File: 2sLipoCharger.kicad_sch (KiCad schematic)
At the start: 21 parts, among them IC1 CN3702, J2 Conn_01x03_Pin, Q2 PMOS, SW1 SW_SPDT

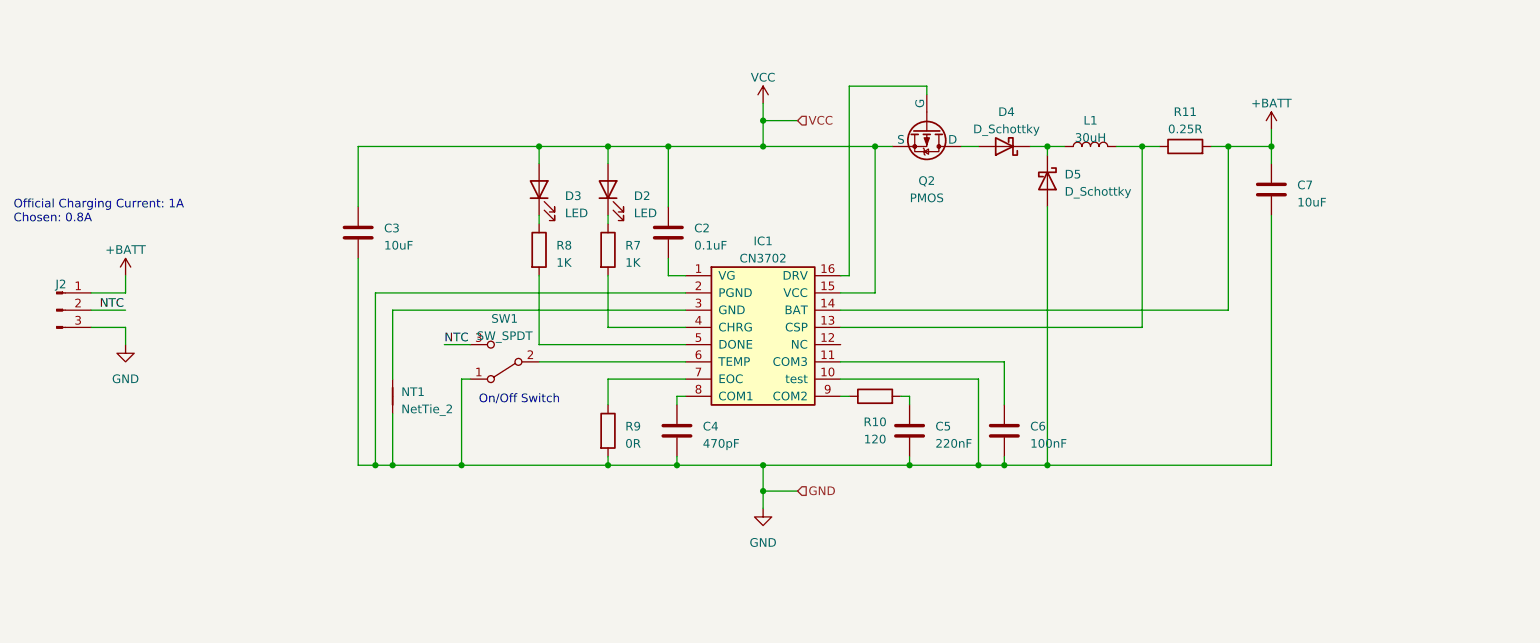
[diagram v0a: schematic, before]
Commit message: Finished Schematic
- Cleaned up page 1
- Only 3 chargers / board now
- LED no longer activated by PG, connected to VCC after the P-MOSFET instead
- Added DC barrel jack for daisy chaining (using M-M 30cm cable)

- Added jumper to enable fast charge
- Selected inductor, diode, P-MOSFET, current sense resistor
- Changed slide switch to 90 degree
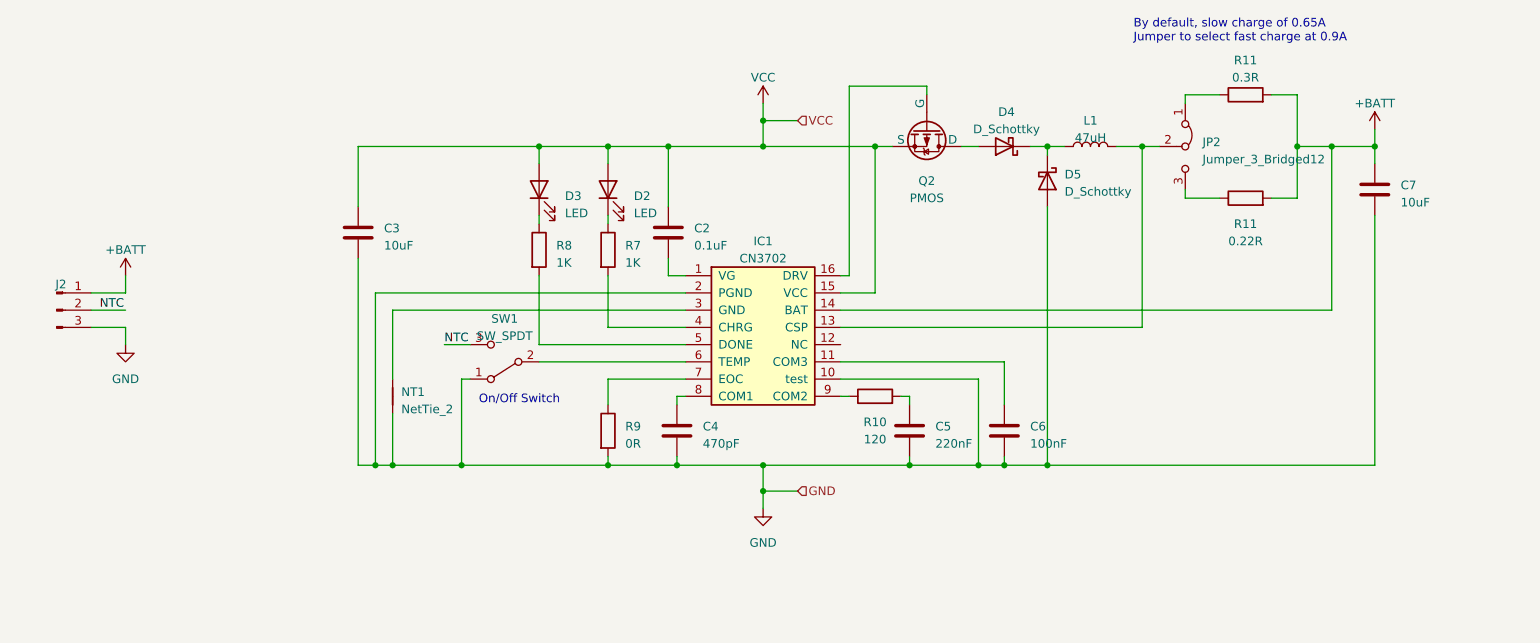
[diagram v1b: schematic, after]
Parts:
- added JP2: Jumper_3_Bridged12, symbol Jumper:Jumper_3_Bridged12
- added R11: 0.22R, symbol Device:R
- D4, D5: JLCPCB Part # (none) -> C8598; Part (none) -> B5819W SL
- L1: value 30uH -> 47uH; JLCPCB Part # (none) -> C497841; Part (none) -> YNR6045-470M
- R11: value 0.25R -> 0.3R; JLCPCB Part # (none) -> C2934256; Part (none) -> FRL0603JR300TS
- SW1: JLCPCB Part # C431544 -> C431541; Part MST22D18G2 -> MSK12C02-HB
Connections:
- net +BATT: now also R11.2
- net at IC1.13 (CSP), L1.2: now also JP2.2 (C); no longer R11.1
- new net: JP2.1 (A), R11.1
- new net: JP2.3 (B), R11.1
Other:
- note added: "By default, slow charge of 0.65A Jumper to select fast charge at 0.9A"
- note removed: "Official Charging Current: 1A Chosen: 0.8A"
- moved on the sheet: C7, R11

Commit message: Footprint assignment partially done
- incomplete: minor edit of footprints, locking pin header footprints
- changed LEDs to side facing, changed PG LED resistor to 4.7k since
  will be going through 20V
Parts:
- C2, C3, C4, C5, C6, C7: footprint (none) -> Capacitor_SMD:C_0603_1608Metric
- D2: footprint (none) -> LED_SMD:LED_0603_1608Metric; JLCPCB Part # (none) -> C965860; Part (none) -> XL-1606SURC
- D3: footprint (none) -> LED_SMD:LED_0603_1608Metric; JLCPCB Part # (none) -> C965863; Part (none) -> XL-1606UGC
- D4, D5: footprint (none) -> Diode_SMD:D_SOD-123
- IC1: footprint (none) -> Package_SO:TSSOP-16_4.4x5mm_P0.65mm
- L1: footprint (none) -> Inductor_SMD:L_Sunlord_SWPA6045S
- Q2: footprint (none) -> Package_TO_SOT_SMD:SOT-23
- R10, R11, R7, R8, R9: footprint (none) -> Resistor_SMD:R_0603_1608Metric
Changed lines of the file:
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@@
       (effects (font (size 1.27 1.27)) (justify left))
     )
-    (property "Footprint" "" (at 238.4552 83.82 0)
+    (property "Footprint" "Capacitor_SMD:C_0603_1608Metric" (at 238.4552 83.82 0)
       (effects (font (size 1.27 1.27)) hide)
     )
@@
       (effects (font (size 1.27 1.27)))
     )
-    (property "Footprint" "" (at 146.05 100.33 0)
+    (property "Footprint" "Package_SO:TSSOP-16_4.4x5mm_P0.65mm" (at 146.05 100.33 0)
       (effects (font (size 1.27 1.27)) hide)
     )
@@
       (effects (font (size 1.27 1.27)))
     )
-    (property "Footprint" "" (at 173.99 76.2 0)
+    (property "Footprint" "Package_TO_SOT_SMD:SOT-23" (at 173.99 76.2 0)
       (effects (font (size 1.27 1.27)) hide)
     )
@@
       (effects (font (size 1.27 1.27)) (justify left))
     )
-    (property "Footprint" "" (at 122.682 115.57 90)
+    (property "Footprint" "Resistor_SMD:R_0603_1608Metric" (at 122.682 115.57 90)
       (effects (font (size 1.27 1.27)) hide)
     )
@@
       (effects (font (size 1.27 1.27)) (justify right))
     )
-    (property "Footprint" "" (at 114.3 80.01 0)
+    (property "Footprint" "LED_SMD:LED_0603_1608Metric" (at 114.3 80.01 0)
       (effects (font (size 1.27 1.27)) hide)
     )
     (property "Datasheet" "~" (at 114.3 80.01 0)
+      (effects (font (size 1.27 1.27)) hide)
+    )
+    (property "Part" "XL-1606UGC" (at 114.3 80.01 90)
+      (effects (font (size 1.27 1.27)) hide)
+    )
+    (property "JLCPCB Part #" "C965863" (at 114.3 80.01 90)
       (effects (font (size 1.27 1.27)) hide)
     )
@@
       (effects (font (size 1.27 1.27)) (justify right))
     )
-    (property "Footprint" "" (at 124.46 80.01 0)
+    (property "Footprint" "LED_SMD:LED_0603_1608Metric" (at 124.46 80.01 0)
       (effects (font (size 1.27 1.27)) hide)
     )
@@
       (effects (font (size 1.27 1.27)) hide)
     )
+    (property "Part" "XL-1606SURC" (at 124.46 80.01 90)
+      (effects (font (size 1.27 1.27)) hide)
+    )
+    (property "JLCPCB Part #" "C965860" (at 124.46 80.01 90)
+      (effects (font (size 1.27 1.27)) hide)
+    )
     (pin "1")
     (pin "2")
@@
       (effects (font (size 1.27 1.27)) (justify left))
     )
-    (property "Footprint" "" (at 134.3152 90.17 0)
+    (property "Footprint" "Capacitor_SMD:C_0603_1608Metric" (at 134.3152 90.17 0)
       (effects (font (size 1.27 1.27)) hide)
     )
@@
       (effects (font (size 1.27 1.27)) (justify left))
     )
-    (property "Footprint" "" (at 88.5952 90.17 0)
+    (property "Footprint" "Capacitor_SMD:C_0603_1608Metric" (at 88.5952 90.17 0)
       (effects (font (size 1.27 1.27)) hide)
     )
@@
       (effects (font (size 1.27 1.27)) (justify left))
     )
-    (property "Footprint" "" (at 169.8752 119.38 0)
+    (property "Footprint" "Capacitor_SMD:C_0603_1608Metric" (at 169.8752 119.38 0)
       (effects (font (size 1.27 1.27)) hide)
     )
@@
       (effects (font (size 1.27 1.27)))
     )
-    (property "Footprint" "" (at 163.83 112.268 90)
+    (property "Footprint" "Resistor_SMD:R_0603_1608Metric" (at 163.83 112.268 90)
       (effects (font (size 1.27 1.27)) hide)
     )
@@
       (effects (font (size 1.27 1.27)) (justify left))
     )
-    (property "Footprint" "" (at 135.5852 119.38 0)
+    (property "Footprint" "Capacitor_SMD:C_0603_1608Metric" (at 135.5852 119.38 0)
       (effects (font (size 1.27 1.27)) hide)
     )
@@
       (effects (font (size 1.27 1.27)) hide)
     )
-    (property "Datasheet" "~" (at 109.22 105.41 0)
+    (property "Datasheet" "https://datasheet.lcsc.com/lcsc/1912111437_SHOU-HAN-MSK12C02-HB_C431541.pdf" (at 109.22 105.41 0)
       (effects (font (size 1.27 1.27)) hide)
     )
@@
       (effects (font (size 1.27 1.27)) (justify left))
     )
-    (property "Footprint" "" (at 112.522 88.9 90)
+    (property "Footprint" "Resistor_SMD:R_0603_1608Metric" (at 112.522 88.9 90)
       (effects (font (size 1.27 1.27)) hide)
     )
@@
       (effects (font (size 1.27 1.27)) (justify left))
     )
-    (property "Footprint" "" (at 122.682 88.9 90)
+    (property "Footprint" "Resistor_SMD:R_0603_1608Metric" (at 122.682 88.9 90)
       (effects (font (size 1.27 1.27)) hide)
     )
@@
       (effects (font (size 1.27 1.27)))
     )
-    (property "Footprint" "" (at 182.88 73.66 0)
+    (property "Footprint" "Diode_SMD:D_SOD-123" (at 182.88 73.66 0)
       (effects (font (size 1.27 1.27)) hide)
     )
@@
       (effects (font (size 1.27 1.27)) (justify left))
     )
-    (property "Footprint" "" (at 183.8452 119.38 0)
+    (property "Footprint" "Capacitor_SMD:C_0603_1608Metric" (at 183.8452 119.38 0)
       (effects (font (size 1.27 1.27)) hide)
     )
@@
       (effects (font (size 1.27 1.27)))
     )
-    (property "Footprint" "" (at 218.44 83.058 90)
+    (property "Footprint" "Resistor_SMD:R_0603_1608Metric" (at 218.44 83.058 90)
       (effects (font (size 1.27 1.27)) hide)
     )
@@
       (effects (font (size 1.27 1.27)))
     )
-    (property "Footprint" "" (at 218.44 67.818 90)
+    (property "Footprint" "Resistor_SMD:R_0603_1608Metric" (at 218.44 67.818 90)
       (effects (font (size 1.27 1.27)) hide)
     )
@@
       (effects (font (size 1.27 1.27)))
     )
-    (property "Footprint" "" (at 195.58 73.66 0)
-      (effects (font (size 1.27 1.27)) hide)
-    )
-    (property "Datasheet" "~" (at 195.58 73.66 0)
+    (property "Footprint" "Inductor_SMD:L_Sunlord_SWPA6045S" (at 195.58 73.66 0)
+      (effects (font (size 1.27 1.27)) hide)
+    )
+    (property "Datasheet" "https://datasheet.lcsc.com/lcsc/2006231815_YJYCOIN-YNR6045-4R7M_C341065.pdf" (at 195.58 73.66 0)
       (effects (font (size 1.27 1.27)) hide)
     )
@@
       (effects (font (size 1.27 1.27)) (justify left))
     )
-    (property "Footprint" "" (at 189.23 78.74 0)
-      (effects (font (size 1.27 1.27)) hide)
-    )
+    (property "Footprint" "Diode_SMD:D_SOD-123" (at 189.23 78.74 0)
+      (effects (font (size 1.27 1.27)) hide)
+    )

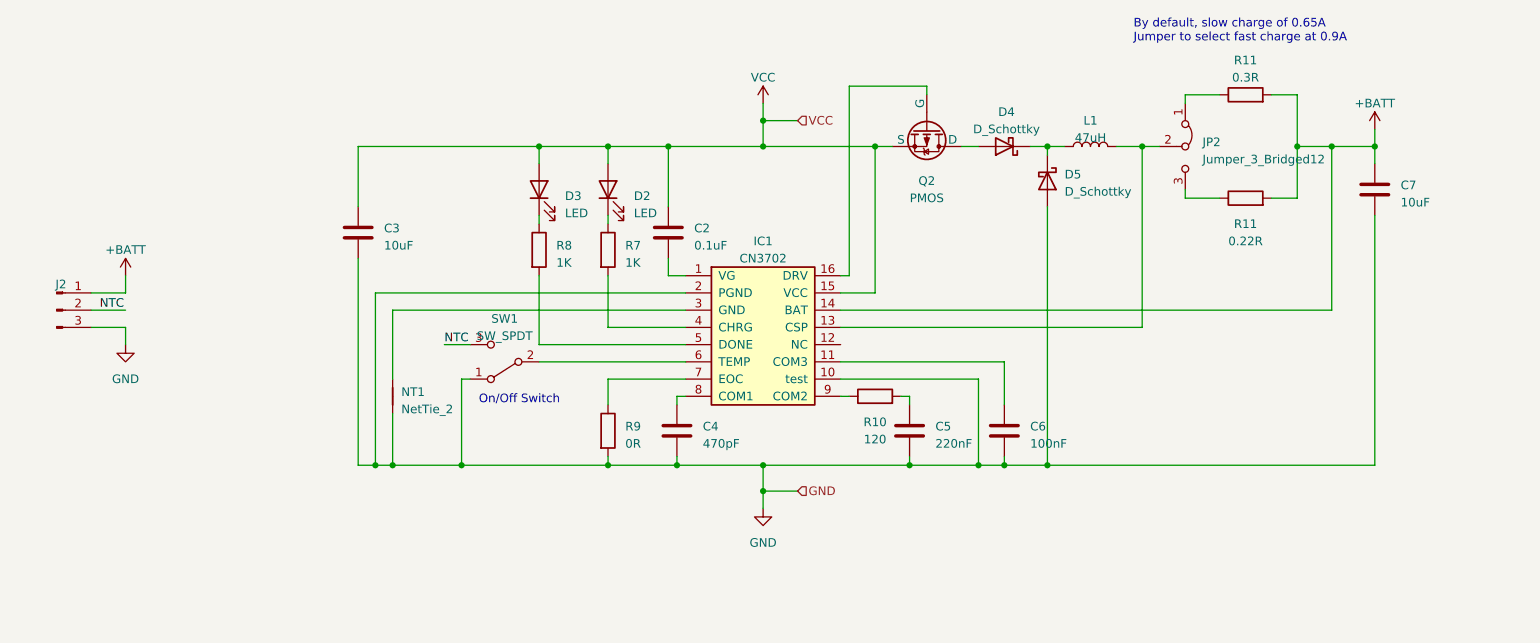
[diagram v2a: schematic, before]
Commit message: Finished footprint assignments, added testpoints
- Added polyfuse
- Cleaned up schematic (mirrored some components for clarity)
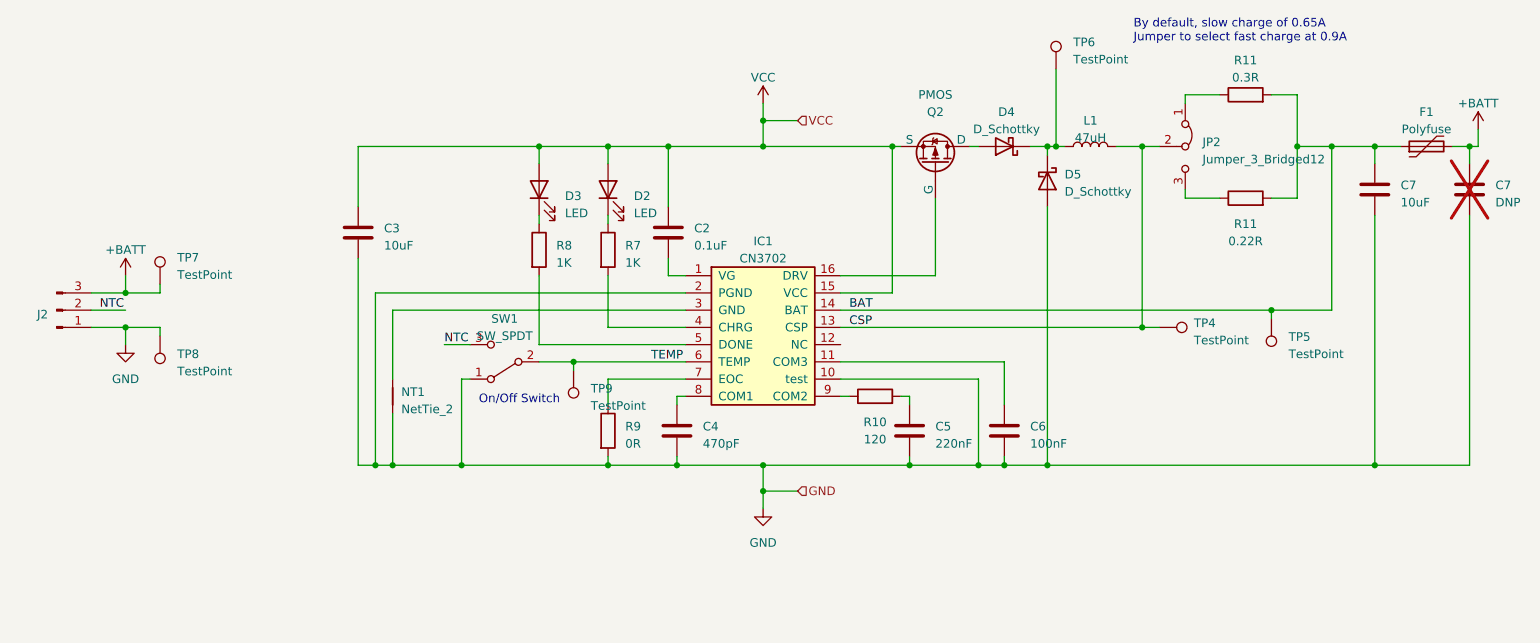
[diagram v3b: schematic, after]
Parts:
- added C7: DNP, Capacitor_SMD:C_0603_1608Metric, symbol Device:C
- added F1: Polyfuse, Resistor_SMD:R_1812_4532Metric, symbol Device:Polyfuse
- added TP4, TP5, TP6, TP7, TP8, TP9: TestPoint, TestPoint:TestPoint_Pad_D2.0mm, symbol Connector:TestPoint
- J2: footprint (none) -> JH:BladeConn_1x03_P2.00mm_Lock; now left out of the parts list
- JP2: footprint (none) -> SparkFun_Connectors:1X03_LOCK; now left out of the parts list
- SW1: footprint (none) -> Button_Switch_SMD:SW_SPDT_PCM12
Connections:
- net +BATT: now also J2.3 (Pin_3), C7.1, F1.2, TP7.1; no longer C7.1, IC1.14 (BAT), J2.1 (Pin_1), R11.2, R11.2
- net GND: now also J2.1 (Pin_1), C7.2, TP8.1; no longer J2.3 (Pin_3)
- net CSP: now reaches IC1.13 (CSP), JP2.2 (C), L1.2
- net CSP: now also TP4.1
- net TEMP: now reaches IC1.6 (TEMP), SW1.2 (B)
- net TEMP: now also TP9.1
- net at D4.1 (K), D5.1 (K), L1.1: now also TP6.1
- new net BAT: C7.1, F1.1, IC1.14 (BAT), R11.2, R11.2, TP5.1
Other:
- moved on the sheet: Q2

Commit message: Edited DRC, started layout
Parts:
- NT1: footprint (none) -> NetTie:NetTie-2_SMD_Pad0.5mm
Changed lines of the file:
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@@
       (effects (font (size 1.27 1.27)) (justify right))
     )
-    (property "Footprint" "" (at 92.71 110.49 0)
+    (property "Footprint" "NetTie:NetTie-2_SMD_Pad0.5mm" (at 92.71 110.49 0)
       (effects (font (size 1.27 1.27)) hide)
     )

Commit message: CH224K Board Layout complete
- Partial layout of CN3702
- Fixed the incorrect NetTie on 2sLipoCharger.kicad_sch (More things are supposed to go to AGND)
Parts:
- TP4, TP5, TP6, TP7, TP8, TP9: footprint TestPoint:TestPoint_Pad_D2.0mm -> TestPoint:TestPoint_Pad_D1.0mm
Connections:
- net GND: no longer C4.2, C5.2, C6.2, IC1.10 (test), R9.2, SW1.1 (A)
- net GNDA: now reaches IC1.3 (GND), NT1.2
- net GNDA: now also C4.2, C5.2, C6.2, IC1.10 (test), R9.2, SW1.1 (A)
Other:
- moved on the sheet: NT1

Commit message: Finished charger layout
- Replace global power symbols in charger schematic with local labels
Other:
- moved on the sheet: TP7, TP8

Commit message: Added tooling and mounting holes
- Added pinout for "done" pin on charger for future use
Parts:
- added J6: Conn_01x01_Pin, Connector_PinHeader_2.54mm:PinHeader_1x01_P2.54mm_Vertical, symbol Connector:Conn_01x01_Pin
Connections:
- net at IC1.5 (DONE), R8.2: now also J6.1 (Pin_1)
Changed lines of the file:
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@@
   (junction (at 124.46 73.66) (diameter 0) (color 0 0 0 0)
   )
+  (junction (at 114.3 93.98) (diameter 0) (color 0 0 0 0)
+  )
   (junction (at 168.91 120.65) (diameter 0) (color 0 0 0 0)
   )
@@
     (stroke (width 0) (type default))
   )
-  (wire (pts (xy 114.3 92.71) (xy 114.3 102.87))
+  (wire (pts (xy 114.3 92.71) (xy 114.3 93.98))
     (stroke (width 0) (type default))
   )
@@
     (stroke (width 0) (type default))
   )
+  (wire (pts (xy 110.49 93.98) (xy 114.3 93.98))
+    (stroke (width 0) (type default))
+  )
   (wire (pts (xy 203.2 100.33) (xy 205.74 100.33))
     (stroke (width 0) (type default))
@@
   )
   (wire (pts (xy 133.35 82.55) (xy 133.35 73.66))
+    (stroke (width 0) (type default))
+  )
+  (wire (pts (xy 114.3 93.98) (xy 114.3 102.87))
     (stroke (width 0) (type default))
   )
@@
         )
       )
+    )
+  )
+  (symbol (lib_id "Connector:Conn_01x01_Pin") (at 105.41 93.98 0) (unit 1)
+    (in_bom yes) (on_board yes) (dnp no) (fields_autoplaced)
+    (property "Reference" "J6" (at 106.045 90.17 0)
+      (effects (font (size 1.27 1.27)))
+    )
+    (property "Value" "Conn_01x01_Pin" (at 106.045 92.71 0)
+      (effects (font (size 1.27 1.27)))
+    )
+    (property "Footprint" "Connector_PinHeader_2.54mm:PinHeader_1x01_P2.54mm_Vertical" (at 105.41 93.98 0)
+      (effects (font (size 1.27 1.27)) hide)
+    )
+    (property "Datasheet" "~" (at 105.41 93.98 0)
+      (effects (font (size 1.27 1.27)) hide)
+    )
+    (pin "1")
+    (instances
+      (project "SPIKE-batt-chg"
+        (path "/40189395-1355-465c-9381-a270b42186bd/67c7df3f-938a-4452-afe2-b5005c69cda5"
+          (reference "J6") (unit 1)
+        )
+        (path "/40189395-1355-465c-9381-a270b42186bd/2ca84df8-0c87-4f75-8a1d-dbe9a9e908fc"
+          (reference "J7") (unit 1)
+        )
+        (path "/40189395-1355-465c-9381-a270b42186bd/7c9abfe4-4b11-404b-8aa4-67235fb7e4c5"
+          (reference "J8") (unit 1)
+        )
+      )

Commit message: Exclude header pins from BOM
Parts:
- J6: now left out of the parts list
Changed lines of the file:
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@@
   )
   (symbol (lib_id "Connector:Conn_01x01_Pin") (at 105.41 93.98 0) (unit 1)
-    (in_bom yes) (on_board yes) (dnp no) (fields_autoplaced)
+    (in_bom no) (on_board yes) (dnp no) (fields_autoplaced)
     (property "Reference" "J6" (at 106.045 90.17 0)
       (effects (font (size 1.27 1.27)))
